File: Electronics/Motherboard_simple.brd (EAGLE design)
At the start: 69.8 x 55.2 mm, 27 parts, among them U2 USD-SOCKETNEW

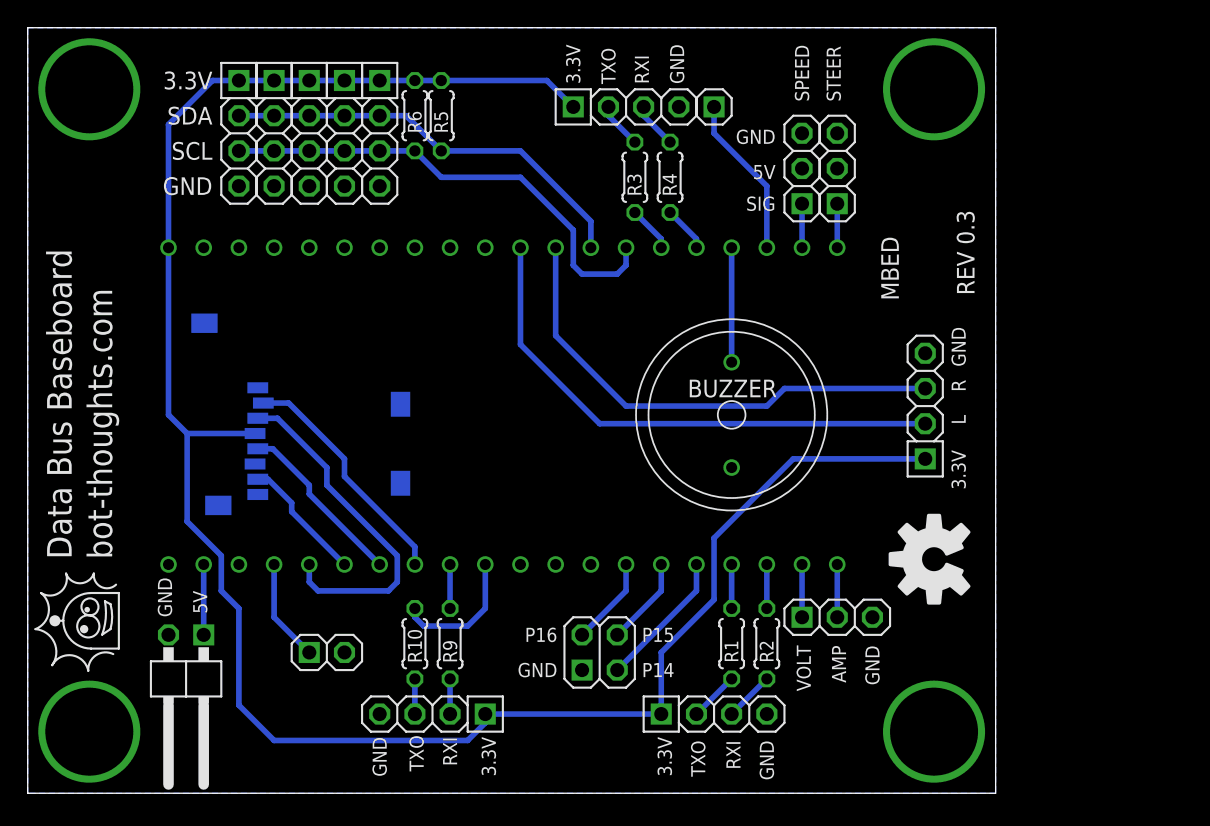
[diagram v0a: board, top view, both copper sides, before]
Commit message: Major revision for through hole, onboard encoder interface.
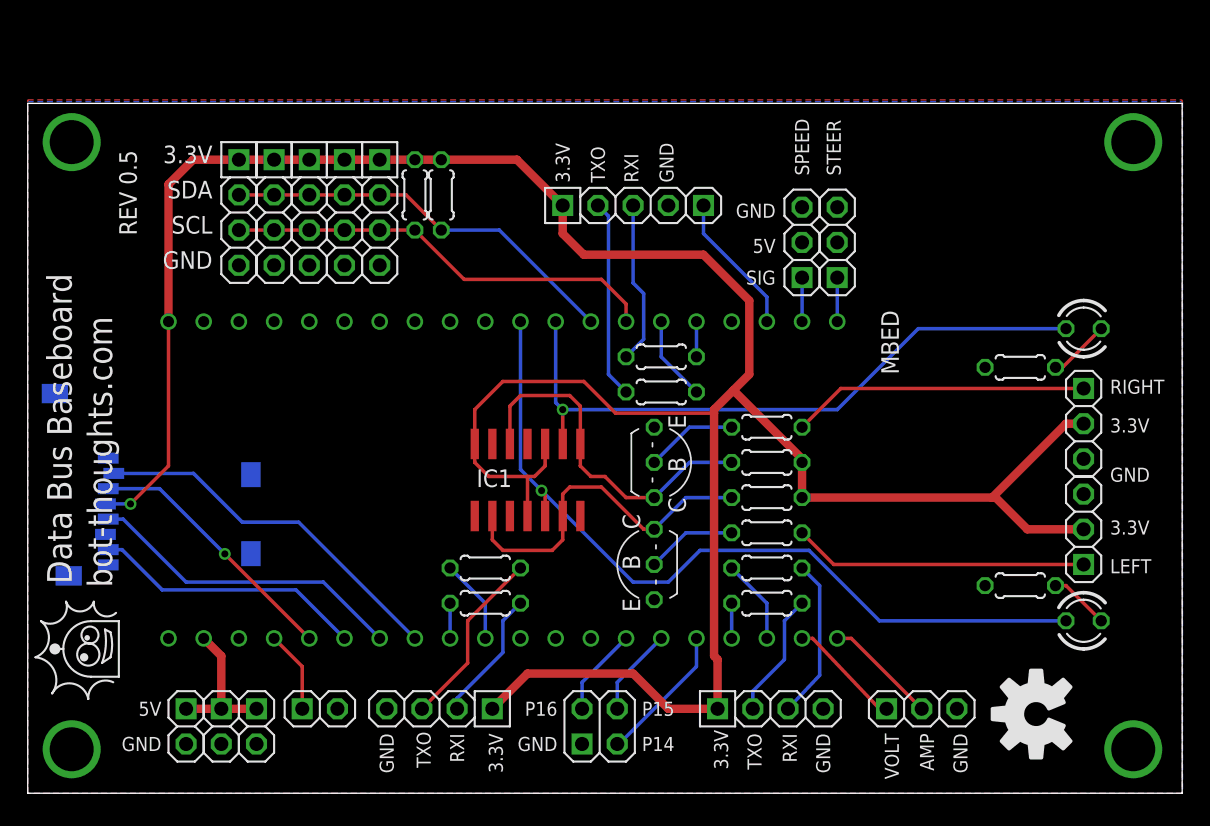
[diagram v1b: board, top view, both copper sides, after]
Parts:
- removed BUZZER: 1438-TWT-R, mes_buzzers:BUZZER_14MM_PTH
- added IC1: NE556D, linear:SO14
- added JP16, JP18: POWER, pinhead-2:1X02-S
- added JP19: ENCODERS, pinhead-2:1X03-S
- added LED_L, LED_R: (no value), led:LED3MM
- added Q1, Q2: 2N3904, mes_transistors:TO92-CBE
- added R11, R12: 10k, rcl:0204/5
- added R13, R14: 1k, rcl:0204/5
- added R7, R8: 330, rcl:0204/5
- JP15: device pinhead-2:1X04-S -> pinhead-2:1X03-S
- JP3: device pinhead-2:1X02/90-S -> pinhead-2:1X02-S
- moved R3 15.6 mm to (45.7, 29.0), turned to 180 degrees
- moved JP15 14.5 mm to (76.2, 19.1)
- moved R4 13.0 mm to (45.7, 31.5), turned to 180 degrees
- moved U2 11.9 mm to (16.5, 15.2)
- moved JP17 8.99 mm to (64.5, 6.10)
- moved R10 7.46 mm to (33.0, 16.3), turned to 0 degrees
- moved JP2 7.15 mm to (42.4, 42.4)
- moved JP7 7.15 mm to (48.8, 42.4)
- moved JP3 6.94 mm to (16.5, 4.83), turned to 270 degrees
- moved JP11 5.72 mm to (20.3, 41.9)
- moved JP12 5.72 mm to (15.2, 41.9)
- moved JP13 5.72 mm to (22.9, 41.9)
- moved JP14 5.72 mm to (17.8, 41.9)
- moved JP5 5.72 mm to (25.4, 41.9)
- moved R5 5.72 mm to (29.8, 43.2)
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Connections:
- new net MCU_LEFT: IC1.5, LED_L.A, MBED.P$30
- new net MCU_RIGHT: IC1.9, LED_R.A, MBED.P$29
- new net N$11: IC1.12, IC1.8, Q2.C, R12.1
- new net N$13: Q2.B, R13.1
- new net N$14: Q1.B, R14.1
- new net N$3: LED_L.K, R7.2
- new net N$4: LED_R.K, R8.2
- net +3V3: now also IC1.10, IC1.14, IC1.4, JP15.2, JP19.2, R11.2, R12.2; no longer JP15.1
- net +5V: now also JP16.1, JP18.1
- net ENC_LEFT: now also JP15.1, R14.2; no longer JP15.2, MBED.P$30
- net ENC_RIGHT: now also JP19.1, R13.2; no longer JP15.3, MBED.P$29
- net GND: now also IC1.7, JP15.3, JP16.2, JP18.2, JP19.3, Q1.E, Q2.E, R7.1, R8.1; no longer BUZZER.P$2, JP15.4
- net N$12: now also IC1.2, IC1.6, Q1.C, R11.1; no longer BUZZER.P$1, MBED.P$24
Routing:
- net MCU_LEFT: track 0.00 -> 58.4 mm, vias 0 -> 1
- net +3V3: track 144.8 -> 196.0 mm, vias 0 -> 1
- net MCU_RIGHT: track 0.00 -> 47.8 mm, vias 0 -> 1
- net N$11: track 0.00 -> 25.7 mm
- net ENC_LEFT: track 38.6 -> 21.3 mm
- net N$12: track 8.26 -> 25.3 mm
- net ENC_RIGHT: track 35.7 -> 21.5 mm
- net N$9: track 3.33 -> 14.3 mm
- net N$17: track 2.54 -> 13.1 mm
- net SCK1: track 12.6 -> 23.2 mm
- net MISO1: track 9.17 -> 19.7 mm
- net !CS1: track 17.2 -> 26.7 mm
- net N$10: track 3.33 -> 11.8 mm
- net N$2: track 3.59 -> 11.6 mm
- net N$16: track 2.54 -> 9.51 mm
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- added copper zone on layer 1, net GND
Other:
- board size 69.8 x 55.2 mm -> 83.3 x 49.8 mm
- board text added: "LEFT"
- board text added: "REV 0.5"
- board text added: "RIGHT"
- board text removed: "L"
- board text removed: "R"
- board text removed: "REV 0.3"

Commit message: Major revision, added RC takeover switch circuitry. Moved encoder interface.
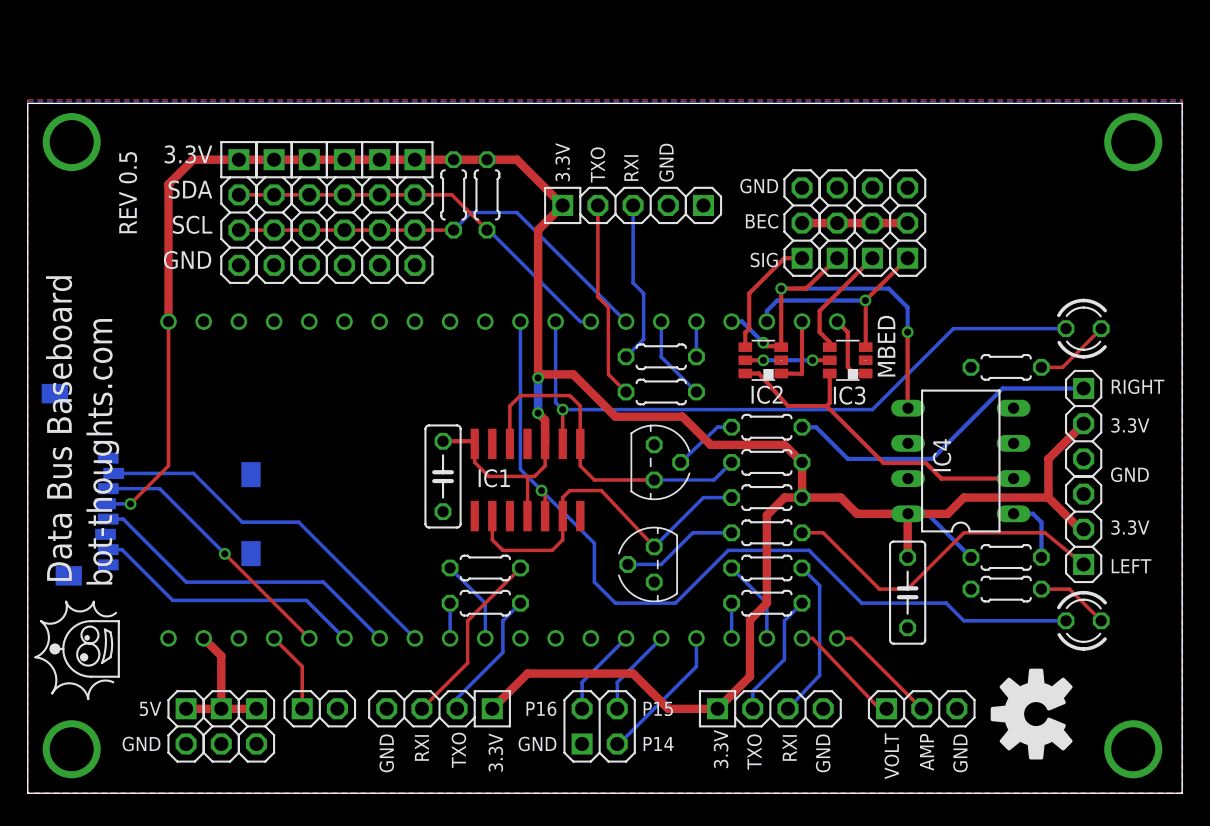
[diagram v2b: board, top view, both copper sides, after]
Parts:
- added C1, C2: 104, rcl:C050-025X075
- added IC2, IC3: 741G3157DBVR, 74xx-little-us:DBV_R-PDSO-G6
- added IC4: TINY25, avr-7:DIL08
- added JP20: I2C, pinhead-2:1X04-S
- added JP21: RXE, pinhead-2:1X03-S
- added JP22: RXS, pinhead-2:1X03-S
- added R15: 10k, rcl:0204/5
- JP8: value SPEED -> ESC
- JP9: value STEER -> SRV
- Q1, Q2: device mes_transistors:TO92-CBE -> mes_transistors:TO92
- moved R5 3.30 mm to (33.1, 43.2)
- moved JP9 2.90 mm to (61.0, 41.1)
- moved R6 2.79 mm to (30.7, 43.2)
- moved JP8 1.40 mm to (55.9, 41.1)
- moved R7 1.05 mm to (70.6, 14.7)
- moved R8 1.02 mm to (70.6, 30.7)
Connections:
- removed net SPEED: JP8.1, MBED.P$22
- removed net STEER: JP9.1, MBED.P$21
- new net BEC: JP21.2, JP22.2, JP8.2, JP9.2
- new net ESC: IC2.4, JP8.1
- new net MCUESC: IC2.1, MBED.P$22
- new net MCUSRV: IC3.1, MBED.P$21
- new net N$15: IC4.1, R15.1
- new net N$25: IC2.6, IC3.6, IC4.2
- new net RXESC: IC2.3, IC4.5, JP21.1, MBED.P$24
- new net RXSRV: IC3.3, JP22.1, MBED.P$23
- new net SRV: IC3.4, JP9.1
- new net VCC: IC2.5, IC3.5
- net +3V3: now also C1.1, C2.1, IC4.8, JP20.1, R15.2
- net GND: now also C1.2, C2.2, IC2.2, IC3.2, IC4.4, JP20.4, JP21.3, JP22.3, Q1.3, Q2.3; no longer Q1.E, Q2.E
- net N$11: now also Q2.1; no longer Q2.C
- net N$12: now also Q1.1; no longer Q1.C
- net N$13: now also Q2.2; no longer Q2.B
- net N$14: now also Q1.2; no longer Q1.B
- net PPS: no longer MBED.P$23
- net SCL: now also JP20.3
- net SDA: now also JP20.2
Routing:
- net RXESC: track 0.00 -> 30.5 mm, vias 0 -> 3
- net N$25: track 0.00 -> 25.0 mm
- net RXSRV: track 0.00 -> 15.9 mm, vias 0 -> 1
- net PPS: track 10.3 -> 0.00 mm
- net ESC: track 0.00 -> 8.86 mm
- net +3V3: track 196.0 -> 187.5 mm, vias 1 -> 3
- net SRV: track 0.00 -> 8.30 mm
- net BEC: track 0.00 -> 7.62 mm
- net VCC: track 0.00 -> 6.10 mm, vias 0 -> 2
- net MCUESC: track 0.00 -> 5.27 mm
- net MCUSRV: track 0.00 -> 5.09 mm
- net N$15: track 0.00 -> 4.80 mm
- net ENC_LEFT: track 21.3 -> 24.5 mm
- net STEER: track 3.17 -> 0.00 mm
- net SPEED: track 3.17 -> 0.00 mm
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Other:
- board text added: "BEC"
- board text removed: "SPEED"
- board text removed: "STEER"

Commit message: Routing tweaks. Added 5V header. Added AVRISP hdr for Tiny
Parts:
- added J1: AVRISP, ads4:CON6P2R
- added JP23: POWER, pinhead-2:1X02-S
- added SJ1, SJ2: (no value), SparkFun:SJ_3
- moved JP7 42.9 mm to (25.9, 6.10), turned to 270 degrees
- moved JP1 5.08 mm to (46.4, 4.83)
- moved JP6 5.08 mm to (58.7, 6.10)
- moved JP17 4.57 mm to (69.1, 6.10)
- moved JP4 2.84 mm to (22.4, 3.56)
- moved JP10 2.54 mm to (32.3, 6.10)
- moved JP21 2.54 mm to (55.9, 41.1)
- moved JP22 2.54 mm to (61.0, 41.1)
- moved JP8 2.54 mm to (53.3, 41.1)
- moved JP9 2.54 mm to (58.4, 41.1)
- moved JP16 1.27 mm to (12.7, 4.83)
- moved JP3 1.27 mm to (15.2, 4.83)
- moved JP18 1.27 mm to (10.2, 4.83)
- moved IC4 0.15 mm to (67.3, 24.1)
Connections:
- removed net N$15: IC4.1, R15.1
- new net !TRST: IC4.1, J1.5, R15.1
- new net MISO: IC4.6, J1.1
- new net N$18: JP10.1, SJ1.2
- new net N$19: JP6.1, SJ2.2
- new net SCK: IC4.7, J1.3
- net +3V3: now also J1.2, SJ1.3, SJ2.3; no longer JP10.1, JP6.1
- net +5V: now also JP23.1, SJ1.1, SJ2.1
- net GND: now also J1.6, JP23.2
- net PPS: now also MBED.P$11
- net RXESC: now also J1.4
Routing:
- net +5V: track 10.7 -> 51.9 mm
- net !TRST: track 0.00 -> 31.0 mm
- net SCK: track 0.00 -> 22.8 mm
- net MISO: track 0.00 -> 18.3 mm, vias 0 -> 1
- net RXESC: track 30.5 -> 44.0 mm, vias 3 -> 1
- net PPS: track 0.00 -> 12.9 mm
- net +3V3: track 187.5 -> 200.3 mm, vias 3 -> 4
- net N$15: track 4.80 -> 0.00 mm
- net AMP: track 8.20 -> 12.8 mm
- net N$6: track 8.28 -> 12.8 mm
- net !RESET: track 5.92 -> 9.07 mm
- net N$18: track 0.00 -> 2.79 mm
- net N$19: track 0.00 -> 2.79 mm
- net ENC_LEFT: track 24.5 -> 21.9 mm
- net RXSRV: track 15.9 -> 18.5 mm, vias 1 -> 2
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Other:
- board text added: "5/3V"

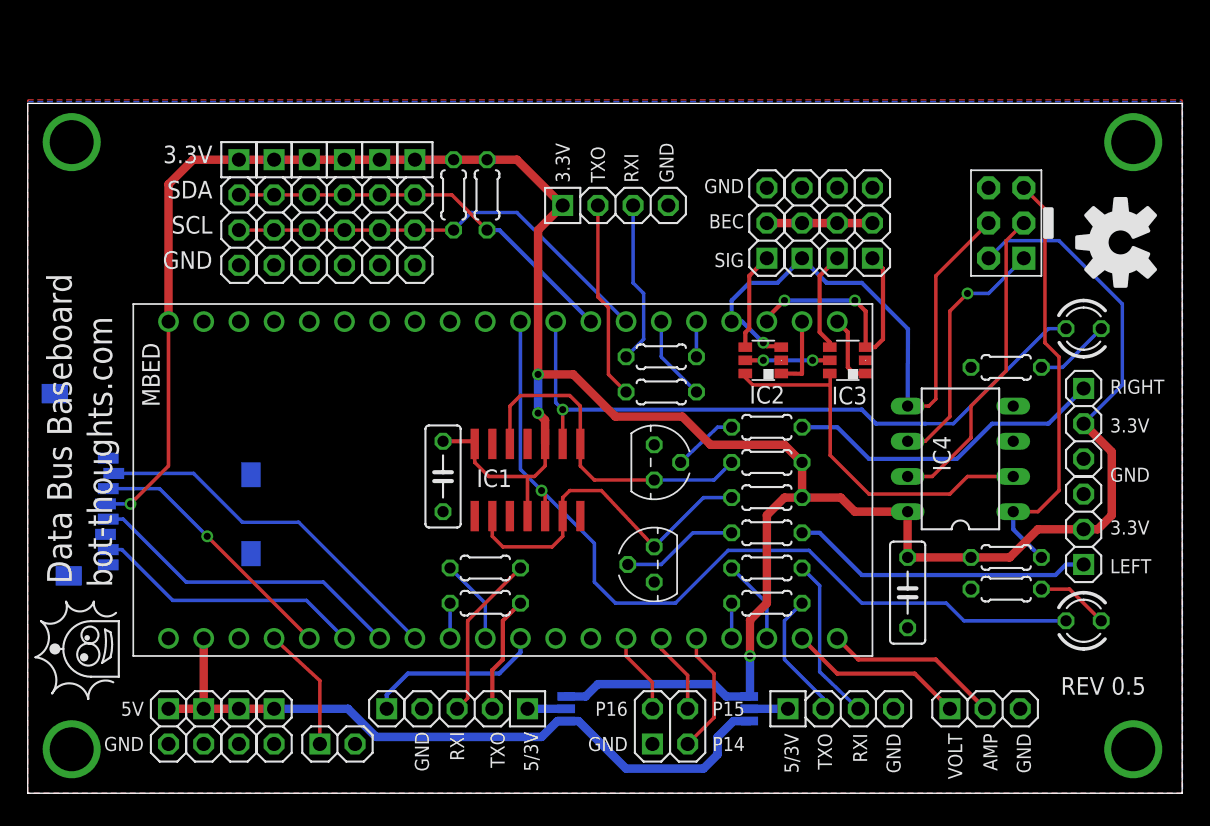
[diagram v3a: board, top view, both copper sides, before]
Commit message: Layout tweaks
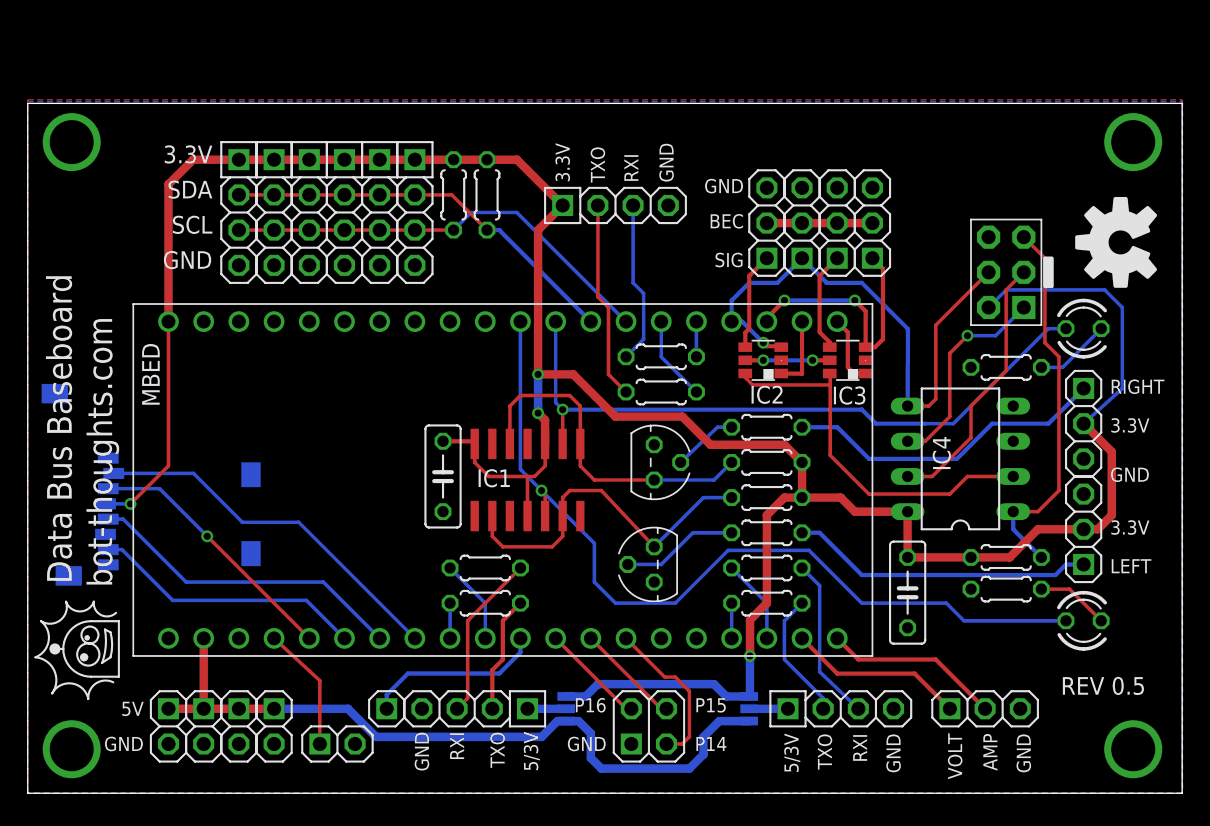
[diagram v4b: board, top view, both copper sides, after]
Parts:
- moved J1 3.56 mm to (70.6, 37.6)
- moved JP1 1.52 mm to (44.8, 4.83)
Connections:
- net N$5: now also JP1.4, MBED.P$13; no longer JP1.2, MBED.P$14
- net N$7: now also JP1.2, MBED.P$12; no longer JP1.4, MBED.P$15
- net N$8: now also MBED.P$14; no longer MBED.P$16
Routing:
- net SCK: track 22.8 -> 19.2 mm
- net RXESC: track 44.0 -> 40.5 mm
- net !TRST: track 31.0 -> 27.4 mm
- net MISO: track 18.3 -> 15.1 mm
- net N$8: track 8.94 -> 11.3 mm
- net N$5: track 5.87 -> 7.57 mm
- net N$7: track 5.87 -> 7.57 mm
- net +3V3: track 200.3 -> 198.7 mm
- net +5V: track 51.9 -> 52.9 mm
